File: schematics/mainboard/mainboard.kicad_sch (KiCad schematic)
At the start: 29 parts, among them J1 Nav Pin, J2 LCD I2C, J3 Serial ESP, J4 RTC DS1307, J5 PWR, J6 Temp DS18B20, J7 Serial ATMega, J8 Relay Module, SW1 Reset ESP, SW2 UART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

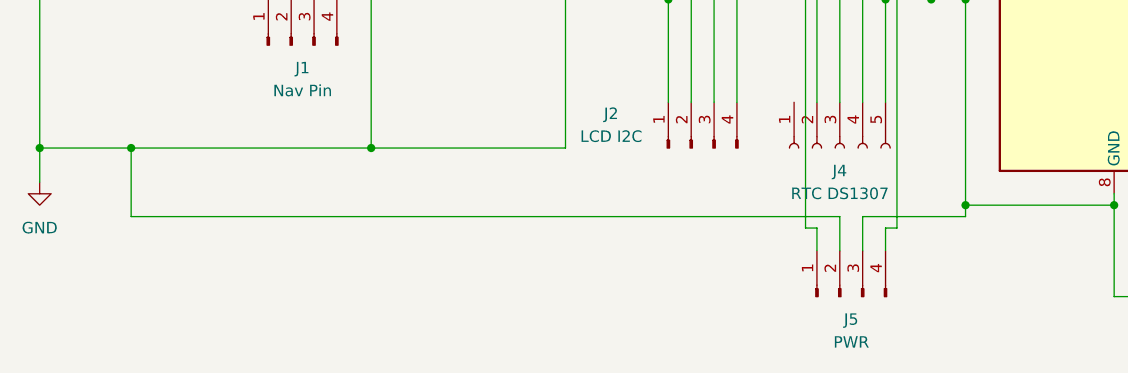
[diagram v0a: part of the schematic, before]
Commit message: fix schematics, added button schematics
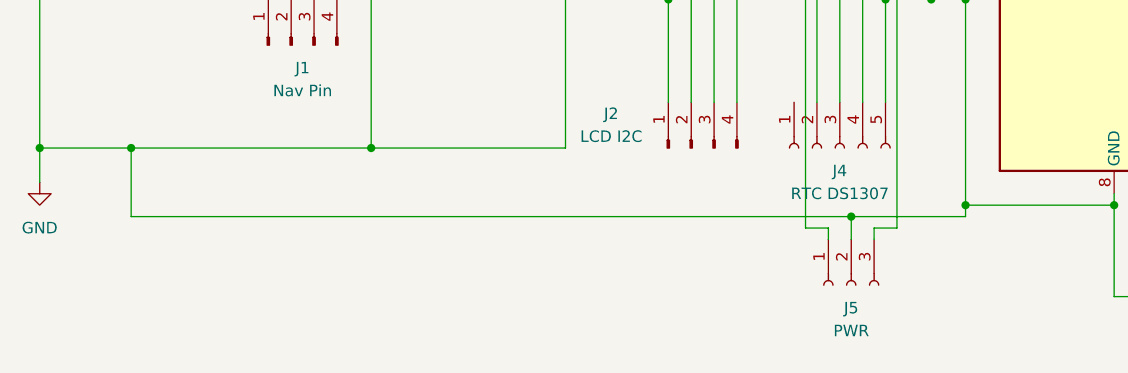
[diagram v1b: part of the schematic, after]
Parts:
- removed J5: PWR, Connector_PinHeader_2.54mm:PinHeader_1x04_P2.54mm_Vertical, symbol Connector:Conn_01x04_Male
- added J5: PWR, TerminalBlock_4Ucon:TerminalBlock_4Ucon_1x03_P3.50mm_Horizontal, symbol Connector:Conn_01x03_Female
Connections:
- net +3.3V: now also J5.1 (Pin_1)
- net +5V: now also J5.3 (Pin_3)
- net GND: now also J5.2 (Pin_2)
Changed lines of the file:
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@@
   (junction (at 114.3 78.74) (diameter 0) (color 0 0 0 0)
   )
+  (junction (at 110.49 102.87) (diameter 0) (color 0 0 0 0)
+  )
   (junction (at 82.55 24.13) (diameter 0) (color 0 0 0 0)
   )
@@
     (stroke (width 0) (type default) (color 0 0 0 0))
   )
-  (wire (pts (xy 111.76 106.68) (xy 111.76 102.87))
-    (stroke (width 0) (type default) (color 0 0 0 0))
-  )
   (wire (pts (xy 45.72 60.96) (xy 45.72 78.74))
     (stroke (width 0) (type default) (color 0 0 0 0))
@@
     (stroke (width 0) (type default) (color 0 0 0 0))
   )
-  (wire (pts (xy 109.22 106.68) (xy 109.22 102.87))
-    (stroke (width 0) (type default) (color 0 0 0 0))
-  )
   (wire (pts (xy 58.42 60.96) (xy 58.42 66.04))
     (stroke (width 0) (type default) (color 0 0 0 0))
@@
     (stroke (width 0) (type default) (color 0 0 0 0))
   )
+  (wire (pts (xy 107.95 104.14) (xy 107.95 105.41))
+    (stroke (width 0) (type default) (color 0 0 0 0))
+  )
   (wire (pts (xy 173.99 82.55) (xy 173.99 111.76))
     (stroke (width 0) (type default) (color 0 0 0 0))
@@
     (stroke (width 0) (type default) (color 0 0 0 0))
   )
-  (wire (pts (xy 114.3 104.14) (xy 115.57 104.14))
-    (stroke (width 0) (type default) (color 0 0 0 0))
-  )
   (wire (pts (xy 157.48 40.64) (xy 157.48 111.76))
     (stroke (width 0) (type default) (color 0 0 0 0))
@@
     (stroke (width 0) (type default) (color 0 0 0 0))
   )
+  (wire (pts (xy 30.48 102.87) (xy 110.49 102.87))
+    (stroke (width 0) (type default) (color 0 0 0 0))
+  )
   (wire (pts (xy 157.48 111.76) (xy 139.7 111.76))
     (stroke (width 0) (type default) (color 0 0 0 0))
@@
     (stroke (width 0) (type default) (color 0 0 0 0))
   )
-  (wire (pts (xy 111.76 102.87) (xy 123.19 102.87))
-    (stroke (width 0) (type default) (color 0 0 0 0))
-  )
   (wire (pts (xy 181.61 74.93) (xy 181.61 86.36))
     (stroke (width 0) (type default) (color 0 0 0 0))
@@
     (stroke (width 0) (type default) (color 0 0 0 0))
   )
-  (wire (pts (xy 106.68 104.14) (xy 105.41 104.14))
-    (stroke (width 0) (type default) (color 0 0 0 0))
-  )
   (wire (pts (xy 158.75 85.09) (xy 154.94 85.09))
     (stroke (width 0) (type default) (color 0 0 0 0))
@@
     (stroke (width 0) (type default) (color 0 0 0 0))
   )
-  (wire (pts (xy 109.22 102.87) (xy 30.48 102.87))
-    (stroke (width 0) (type default) (color 0 0 0 0))
-  )
   (wire (pts (xy 154.94 67.31) (xy 129.54 67.31))
     (stroke (width 0) (type default) (color 0 0 0 0))
   )
+  (wire (pts (xy 105.41 104.14) (xy 107.95 104.14))
+    (stroke (width 0) (type default) (color 0 0 0 0))
+  )
   (wire (pts (xy 48.26 78.74) (xy 48.26 67.31))
     (stroke (width 0) (type default) (color 0 0 0 0))
@@
     (stroke (width 0) (type default) (color 0 0 0 0))
   )
+  (wire (pts (xy 115.57 104.14) (xy 113.03 104.14))
+    (stroke (width 0) (type default) (color 0 0 0 0))
+  )
   (wire (pts (xy 114.3 78.74) (xy 114.3 90.17))
     (stroke (width 0) (type default) (color 0 0 0 0))
@@
     (stroke (width 0) (type default) (color 0 0 0 0))
   )
+  (wire (pts (xy 110.49 102.87) (xy 110.49 105.41))
+    (stroke (width 0) (type default) (color 0 0 0 0))
+  )
   (wire (pts (xy 95.25 67.31) (xy 95.25 90.17))
     (stroke (width 0) (type default) (color 0 0 0 0))
@@
     (stroke (width 0) (type default) (color 0 0 0 0))
   )
-  (wire (pts (xy 106.68 106.68) (xy 106.68 104.14))
-    (stroke (width 0) (type default) (color 0 0 0 0))
-  )
-  (wire (pts (xy 114.3 106.68) (xy 114.3 104.14))
+  (wire (pts (xy 113.03 104.14) (xy 113.03 105.41))
     (stroke (width 0) (type default) (color 0 0 0 0))
   )
   (wire (pts (xy 173.99 80.01) (xy 176.53 80.01))
+    (stroke (width 0) (type default) (color 0 0 0 0))
+  )
+  (wire (pts (xy 123.19 102.87) (xy 110.49 102.87))
     (stroke (width 0) (type default) (color 0 0 0 0))
   )
@@
     (pin "1")
     (pin "2")
+  )
+  (symbol (lib_id "Connector:Conn_01x03_Female") (at 110.49 110.49 90) (mirror x) (unit 1)
+    (in_bom yes) (on_board yes) (fields_autoplaced)
+    (property "Reference" "J5" (id 0) (at 110.49 113.03 90))
+    (property "Value" "PWR" (id 1) (at 110.49 115.57 90))
+    (property "Footprint" "TerminalBlock_4Ucon:TerminalBlock_4Ucon_1x03_P3.50mm_Horizontal" (id 2) (at 110.49 110.49 0)
+      (effects (font (size 1.27 1.27)) hide)
+    )
+    (property "Datasheet" "~" (id 3) (at 110.49 110.49 0)
+      (effects (font (size 1.27 1.27)) hide)
+    )
+    (pin "1")
+    (pin "2")
+    (pin "3")
   )
   (symbol (lib_id "power:+5V") (at 92.71 21.59 0) (unit 1)
@@
     (pin "2")
   )
-  (symbol (lib_id "Connector:Conn_01x04_Male") (at 109.22 111.76 90) (unit 1)
-    (in_bom yes) (on_board yes) (fields_autoplaced)
-    (property "Reference" "J5" (id 0) (at 110.49 114.3 90))
-    (property "Value" "PWR" (id 1) (at 110.49 116.84 90))
-    (property "Footprint" "Connector_PinHeader_2.54mm:PinHeader_1x04_P2.54mm_Vertical" (id 2) (at 109.22 111.76 0)
-      (effects (font (size 1.27 1.27)) hide)
-    )
-    (property "Datasheet" "~" (id 3) (at 109.22 111.76 0)
-      (effects (font (size 1.27 1.27)) hide)
-    )
-    (pin "1")
-    (pin "2")
-    (pin "3")
-    (pin "4")
-  )
   (symbol (lib_id "Device:R") (at 176.53 105.41 0) (unit 1)
     (in_bom yes) (on_board yes) (fields_autoplaced)
@@
       (reference "J4") (unit 1) (value "RTC DS1307") (footprint "Connector_PinSocket_2.54mm:PinSocket_1x05_P2.54mm_Vertical")
     )
-    (path "/f3178d93-9d3d-47c8-8039-61005facee06"
-      (reference "J5") (unit 1) (value "PWR") (footprint "Connector_PinHeader_2.54mm:PinHeader_1x04_P2.54mm_Vertical")
+    (path "/328e2a4a-8f6f-4070-833f-cf97358cac2c"
+      (reference "J5") (unit 1) (value "PWR") (footprint "TerminalBlock_4Ucon:TerminalBlock_4Ucon_1x03_P3.50mm_Horizontal")
     )
     (path "/8dec3aa9-4c4d-49c6-aefb-48450ebaa151"

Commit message: cleanup, added net labels
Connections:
- net DQ: now reaches J6.2 (Pin_2), R6.1, U2.4 (PD2)
- net SDA: now reaches J2.3 (Pin_3), J4.3 (Pin_3), R2.2, U1.19 (GPIO4), U2.27 (PC4)
- net SCL: now reaches J2.4 (Pin_4), J4.2 (Pin_2), R5.2, U1.20 (GPIO5), U2.28 (PC5)
- net TX: now reaches J3.1 (Pin_1), U1.21 (GPIO3/RXD)
- net TX: now also J7.1 (Pin_1), U2.2 (PD0)
- net RX: now reaches J3.2 (Pin_2), U1.22 (GPIO1/TXD)
- net RX: now also J7.2 (Pin_2), U2.3 (PD1)
- net UP: now reaches J1.1 (Pin_1), U1.5 (GPIO14)
- net DOWN: now reaches J1.2 (Pin_2), U1.6 (GPIO12)
- net SET: now reaches J1.3 (Pin_3), U1.7 (GPIO13)
- net CH2: now reaches J8.2 (Pin_2), R10.1, U2.13 (PD7)
- net CH3: now reaches J8.3 (Pin_3), R9.1, U2.14 (PB0)
- net CH1: now reaches J8.1 (Pin_1), R11.1, U2.6 (PD4)
- net OS: now reaches J4.1 (Pin_1)
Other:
- note added: "PUMP"
- note added: "RX"
- note added: "TX"
- note added: "VALVE TEMP"
- note added: "VALVE TIMER"
- moved on the sheet: J5, J7, J8

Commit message: minor fix schematics
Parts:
- C1, C2, C3, C4: footprint Capacitor_THT:C_Disc_D4.3mm_W1.9mm_P5.00mm -> Capacitor_THT:C_Disc_D4.7mm_W2.5mm_P5.00mm
- J5: footprint TerminalBlock_4Ucon:TerminalBlock_4Ucon_1x03_P3.50mm_Horizontal -> TerminalBlock:TerminalBlock_bornier-3_P5.08mm
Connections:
- net RX renamed RX_ATMega
- net RX_ATMega: no longer J3.2 (Pin_2), U1.22 (GPIO1/TXD)
- net TX renamed TX_ATMega
- net TX_ATMega: no longer J3.1 (Pin_1), U1.21 (GPIO3/RXD)
- new net RX_ESP: J3.2 (Pin_2), U1.22 (GPIO1/TXD)
- new net TX_ESP: J3.1 (Pin_1), U1.21 (GPIO3/RXD)
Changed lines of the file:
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@@
     (effects (font (size 1.27 1.27)) (justify left bottom))
   )
-  (label "RX" (at 96.52 60.96 270)
+  (label "RX_ESP" (at 96.52 60.96 270)
     (effects (font (size 1.27 1.27)) (justify right bottom))
   )
@@
     (effects (font (size 1.27 1.27)) (justify left bottom))
   )
-  (label "RX" (at 187.96 68.58 180)
+  (label "RX_ATMega" (at 187.96 68.58 180)
     (effects (font (size 1.27 1.27)) (justify right bottom))
   )
@@
     (effects (font (size 1.27 1.27)) (justify left bottom))
   )
-  (label "TX" (at 187.96 66.04 180)
+  (label "TX_ATMega" (at 187.96 66.04 180)
     (effects (font (size 1.27 1.27)) (justify right bottom))
   )
@@
     (effects (font (size 1.27 1.27)) (justify left bottom))
   )
-  (label "TX" (at 99.06 60.96 270)
+  (label "TX_ESP" (at 99.06 60.96 270)
     (effects (font (size 1.27 1.27)) (justify right bottom))
   )
@@
     (property "Reference" "J5" (id 0) (at 110.49 116.84 90))
     (property "Value" "PWR" (id 1) (at 110.49 119.38 90))
-    (property "Footprint" "TerminalBlock_4Ucon:TerminalBlock_4Ucon_1x03_P3.50mm_Horizontal" (id 2) (at 110.49 114.3 0)
+    (property "Footprint" "TerminalBlock:TerminalBlock_bornier-3_P5.08mm" (id 2) (at 110.49 114.3 0)
       (effects (font (size 1.27 1.27)) hide)
     )
@@
       (effects (font (size 1.27 1.27)) (justify left))
     )
-    (property "Footprint" "Capacitor_THT:C_Disc_D4.3mm_W1.9mm_P5.00mm" (id 2) (at 161.29 107.95 0)
+    (property "Footprint" "Capacitor_THT:C_Disc_D4.7mm_W2.5mm_P5.00mm" (id 2) (at 161.29 107.95 0)
       (effects (font (size 1.27 1.27)) hide)
     )
@@
       (effects (font (size 1.27 1.27)) (justify left))
     )
-    (property "Footprint" "Capacitor_THT:C_Disc_D4.3mm_W1.9mm_P5.00mm" (id 2) (at 119.38 48.26 0)
+    (property "Footprint" "Capacitor_THT:C_Disc_D4.7mm_W2.5mm_P5.00mm" (id 2) (at 119.38 48.26 0)
       (effects (font (size 1.27 1.27)) hide)
     )
@@
       (effects (font (size 1.27 1.27)) (justify left))
     )
-    (property "Footprint" "Capacitor_THT:C_Disc_D4.3mm_W1.9mm_P5.00mm" (id 2) (at 124.46 38.1 0)
+    (property "Footprint" "Capacitor_THT:C_Disc_D4.7mm_W2.5mm_P5.00mm" (id 2) (at 124.46 38.1 0)
       (effects (font (size 1.27 1.27)) hide)
     )
@@
       (effects (font (size 1.27 1.27)) (justify left))
     )
-    (property "Footprint" "Capacitor_THT:C_Disc_D4.3mm_W1.9mm_P5.00mm" (id 2) (at 168.91 107.95 0)
+    (property "Footprint" "Capacitor_THT:C_Disc_D4.7mm_W2.5mm_P5.00mm" (id 2) (at 168.91 107.95 0)
       (effects (font (size 1.27 1.27)) hide)
     )
@@
     )
     (path "/65595aa7-553e-408f-bb71-b72bb2eb45b1"
-      (reference "C1") (unit 1) (value "100nf") (footprint "Capacitor_THT:C_Disc_D4.3mm_W1.9mm_P5.00mm")
+      (reference "C1") (unit 1) (value "100nf") (footprint "Capacitor_THT:C_Disc_D4.7mm_W2.5mm_P5.00mm")
     )
     (path "/9f151ca1-3475-4d00-bce9-141148bbc46c"
-      (reference "C2") (unit 1) (value "100nf") (footprint "Capacitor_THT:C_Disc_D4.3mm_W1.9mm_P5.00mm")
+      (reference "C2") (unit 1) (value "100nf") (footprint "Capacitor_THT:C_Disc_D4.7mm_W2.5mm_P5.00mm")
     )
     (path "/5d052e58-d902-4a02-8746-66fb492f8f77"
-      (reference "C3") (unit 1) (value "22pf") (footprint "Capacitor_THT:C_Disc_D4.3mm_W1.9mm_P5.00mm")
+      (reference "C3") (unit 1) (value "22pf") (footprint "Capacitor_THT:C_Disc_D4.7mm_W2.5mm_P5.00mm")
     )
     (path "/fd253808-ef41-4046-a5c4-e485fe534245"
-      (reference "C4") (unit 1) (value "22pf") (footprint "Capacitor_THT:C_Disc_D4.3mm_W1.9mm_P5.00mm")
+      (reference "C4") (unit 1) (value "22pf") (footprint "Capacitor_THT:C_Disc_D4.7mm_W2.5mm_P5.00mm")
     )
     (path "/85d257cb-70d4-4e9d-9e5e-aeb837df84c3"
@@
     )
     (path "/328e2a4a-8f6f-4070-833f-cf97358cac2c"
-      (reference "J5") (unit 1) (value "PWR") (footprint "TerminalBlock_4Ucon:TerminalBlock_4Ucon_1x03_P3.50mm_Horizontal")
+      (reference "J5") (unit 1) (value "PWR") (footprint "TerminalBlock:TerminalBlock_bornier-3_P5.08mm")
     )
     (path "/8dec3aa9-4c4d-49c6-aefb-48450ebaa151"
